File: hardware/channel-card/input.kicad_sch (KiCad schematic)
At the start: 50 parts, among them J1 INPUT MODULE, SW1 LOW-CUT (latching), U1 AD8273, U2 NE5532, U3 NE5532, U4 DG413DY

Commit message: Redraw filter and input sheets with wires; low-cut to 100 Hz
Filter and Input sheets are now drawn with real wires inside each
circuit block, generated by filter_wired.py and input_wired.py and
checked pin by pin against reference netlists (the Input reference is
frozen in scripts/reference). SSI2144 symbol rearranged so the ladder
capacitors sit beside their pins. Obsolete label-only post scripts
removed. The input low-cut moves to 100 Hz with 24k/47k resistors
(decision 73).

Co-Authored-By: Claude Opus 5.5 <noreply@anthropic.com>
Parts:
- R11, R13: value 16k -> 24k; ProjectPN SX-R-005 -> SX-R-031
- R12, R14: value 33k -> 47k; ProjectPN SX-R-006 -> SX-R-032
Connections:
- net LC_LED: no longer names the net of D5.2 (A), R18.2
- net LC_LEDK: no longer names the net of D5.1 (K), SW1.4 (A)
- net L_CPL: no longer names the net of C5.2, R5.1
- net L_HA: no longer names the net of C10.1, C9.2, R11.1
- net L_HB: no longer names the net of C10.2, R12.1, U3.3 (+)
- net L_HP: no longer names the net of R11.2, U3.1, U3.2 (-), U4.3
- net L_N: no longer names the net of C2.1, R2.2, U1.3 (+INA)
- net L_P: no longer names the net of C1.1, R1.2, U1.2 (-INA)
- net L_RX: no longer names the net of C5.1, U1.12 (SENSEA), U1.13 (OUTA)
- net L_SUM: no longer names the net of C7.1, D2.1 (K), R5.2, R7.1, U2.2 (-)
- net L_Z: no longer names the net of D1.1 (K), R9.2
- net R_CPL: no longer names the net of C6.2, R6.1
- net R_HA: no longer names the net of C11.2, C12.1, R13.1
- net R_HB: no longer names the net of C12.2, R14.1, U3.5 (+)
- net R_HP: no longer names the net of R13.2, U3.6 (-), U3.7, U4.6
- net R_N: no longer names the net of C4.1, R4.2, U1.5 (+INB)
- net R_P: no longer names the net of C3.1, R3.2, U1.6 (-INB)
- net R_RX: no longer names the net of C6.1, U1.10 (SENSEB), U1.9 (OUTB)
- net R_SUM: no longer names the net of C8.1, D4.1 (K), R6.2, R8.1, U2.6 (-)
- net R_Z: no longer names the net of D3.1 (K), R10.2
- no-connect marks 4 -> 6

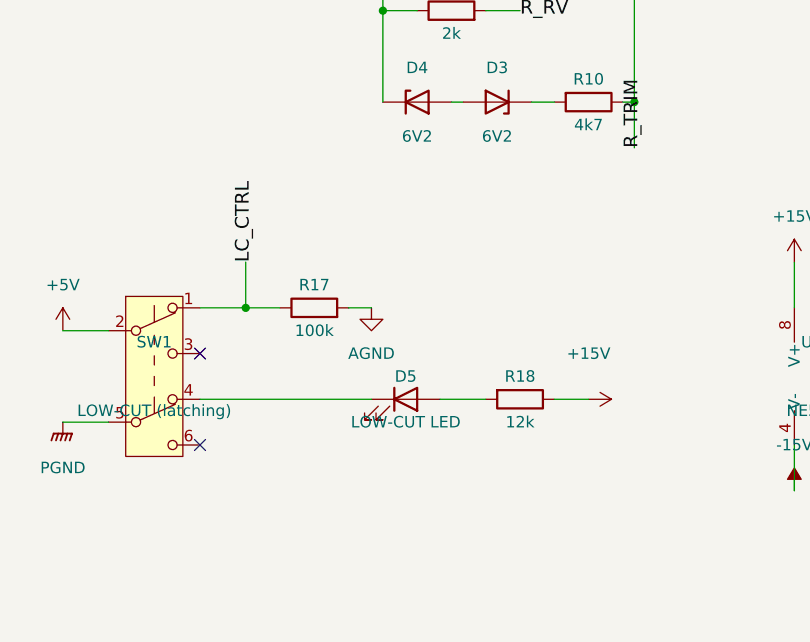
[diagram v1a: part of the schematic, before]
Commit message: Choose GPBS850N latching buttons with printed light caps
Buttons are CW Industries GPBS850N latching DPDT switches (Electrokit)
with 0805 LEDs lighting 3D-printed translucent caps (decision 75).
The datasheet shows pins 2-3 and 5-6 close when pressed, so every
button now uses pin 3 for logic and pin 6 for the LED. Adds the switch
footprint library, rebuild_all.sh, the state-retention requirement for
the momentary-button backlog item, and ten switches to the second
Electrokit order.

Co-Authored-By: Claude Opus 5.5 <noreply@anthropic.com>
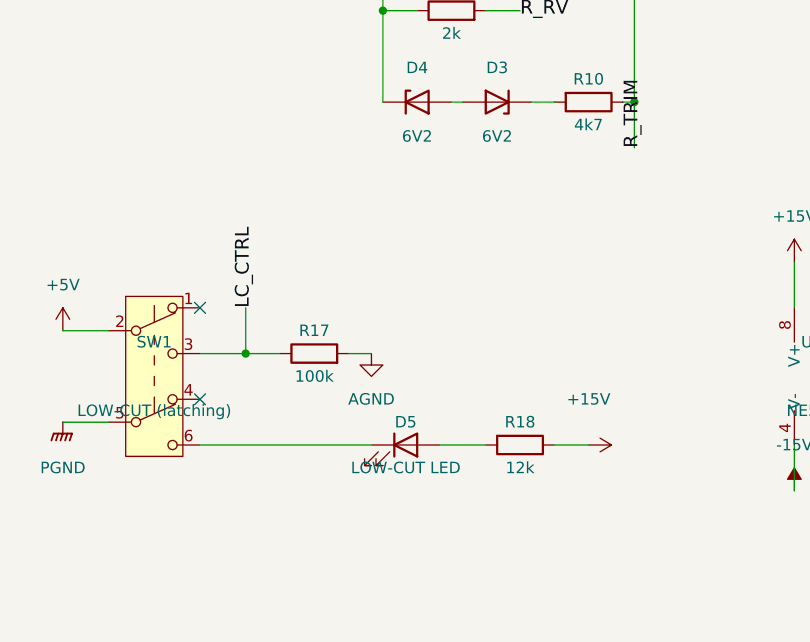
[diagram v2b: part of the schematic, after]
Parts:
- D5: footprint LED_THT:LED_D3.0mm -> LED_SMD:LED_0805_2012Metric
- SW1: footprint (none) -> syntsamix:SW_Latching_8.5x8.5mm_CW_GPBS850N; MPN (none) -> GPBS850N; Manufacturer (none) -> CW Industries; Supplier (none) -> Electrokit; SupplierPN (none) -> 41012905
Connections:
- net LC_CTRL: now also SW1.3 (C); no longer SW1.1 (A)
- net at D5.1 (K): now also SW1.6 (C); no longer SW1.4 (A)

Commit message: Add test pads to the channel card sheets
24 bare 1.5 mm test pads on key audio, control and ground nets across
the Input, Filter, Level, Routing and Meter sheets, named by net and
kept out of the BOM (decision 77). Each pad is in the reference
netlists, so the checks prove it sits on the intended net.

Co-Authored-By: Claude Opus 5.5 <noreply@anthropic.com>
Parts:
- added TP1: L_RX, TestPoint:TestPoint_Pad_D1.5mm, symbol Connector:TestPoint
- added TP2: L_TRIM, TestPoint:TestPoint_Pad_D1.5mm, symbol Connector:TestPoint
- added TP3: L_PREFILT, TestPoint:TestPoint_Pad_D1.5mm, symbol Connector:TestPoint
- added TP4: R_RX, TestPoint:TestPoint_Pad_D1.5mm, symbol Connector:TestPoint
- added TP5: R_TRIM, TestPoint:TestPoint_Pad_D1.5mm, symbol Connector:TestPoint
- added TP6: R_PREFILT, TestPoint:TestPoint_Pad_D1.5mm, symbol Connector:TestPoint
- added TP7: AGND, TestPoint:TestPoint_Pad_D1.5mm, symbol Connector:TestPoint
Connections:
- net AGND: now also TP7.1
- net L_PREFILT: now also TP3.1
- net L_TRIM: now also TP2.1
- net R_PREFILT: now also TP6.1
- net R_TRIM: now also TP5.1
- net at C5.1, U1.12 (SENSEA), U1.13 (OUTA): now also TP1.1
- net at C6.1, U1.10 (SENSEB), U1.9 (OUTB): now also TP4.1

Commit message: Channel card: draw decisions 97 and 98, fader buffer on an OPA2171 (decision 102)
- Level: SC_ENV into the summer's virtual earth through R217 30k1, R218 removed,
  summer + input on AGND (decision 97)
- Q301 emitter and button pull-downs R17, R186, R220, R222, R313, R315, R317 to PGND (decision 98)
- U204 = OPA2171 for the fader buffer and control summer (input range includes V-);
  superdiodes moved to the TL072 U205 (decision 102)
- simulation/level: fader law within 1.2 dB, ducking 10.07 dB per -1 V at every fader position
- Power budget, parts list, STATUS, breadboard test 10 and working notes updated

Co-Authored-By: Claude Opus 5.5 <noreply@anthropic.com>
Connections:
- net AGND: no longer R17.2
- net PGND: now also R17.2

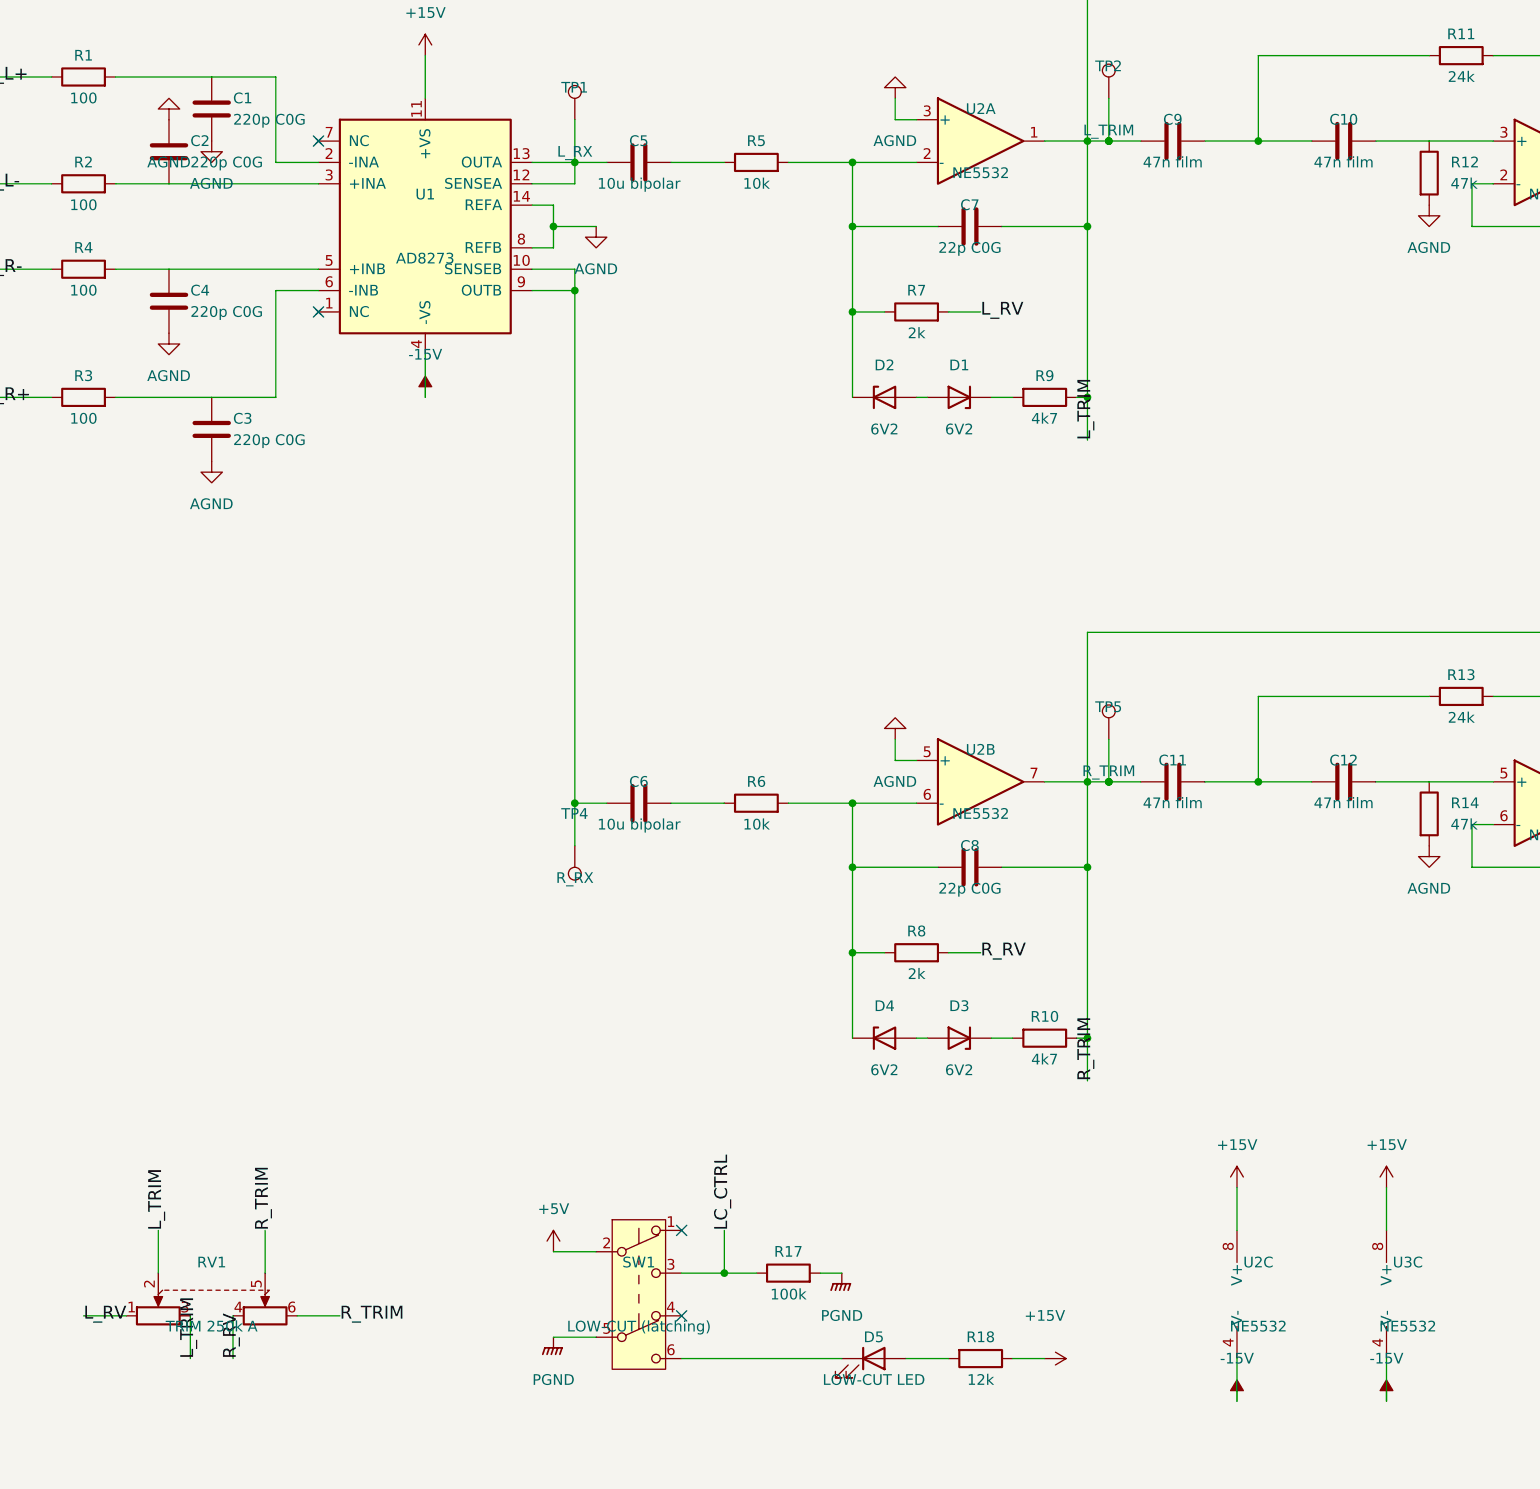
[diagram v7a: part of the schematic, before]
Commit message: Channel card: mechanical parts, decisions 110-117
- 110 LM317/LM337 in D2PAK on copper (onsemi, LCSC)
- 111 SMD electrolytics <= 5.4 mm (ROQANG, Panasonic bipolar)
- 112 trimmers and jumper headers on the underside, bottom cover for /system
- 113 low-cut caps C0G 1206
- 114 pot shaft standard T18 15 mm; 115 trim stage scaled to 100k, pots chosen
  (blocked until RoHS declarations)
- 116 RoHS strict for every part and board (process)
- 117 button LED colours (JLCPCB basic 0805), Wurth chain headers
- J181 drawn as Thonkiconn 3.5 mm (pending /system), fields and footprints set,
  five sheets rebuilt, netlists match, ERC 0/0
- STATUS: seven For /system items (CV jack, 0805 meter bezel, panel screws,
  bottom cover, underside keep-out, RoHS invariant, contract doc updates)

Co-Authored-By: Claude Opus 5.5 <noreply@anthropic.com>
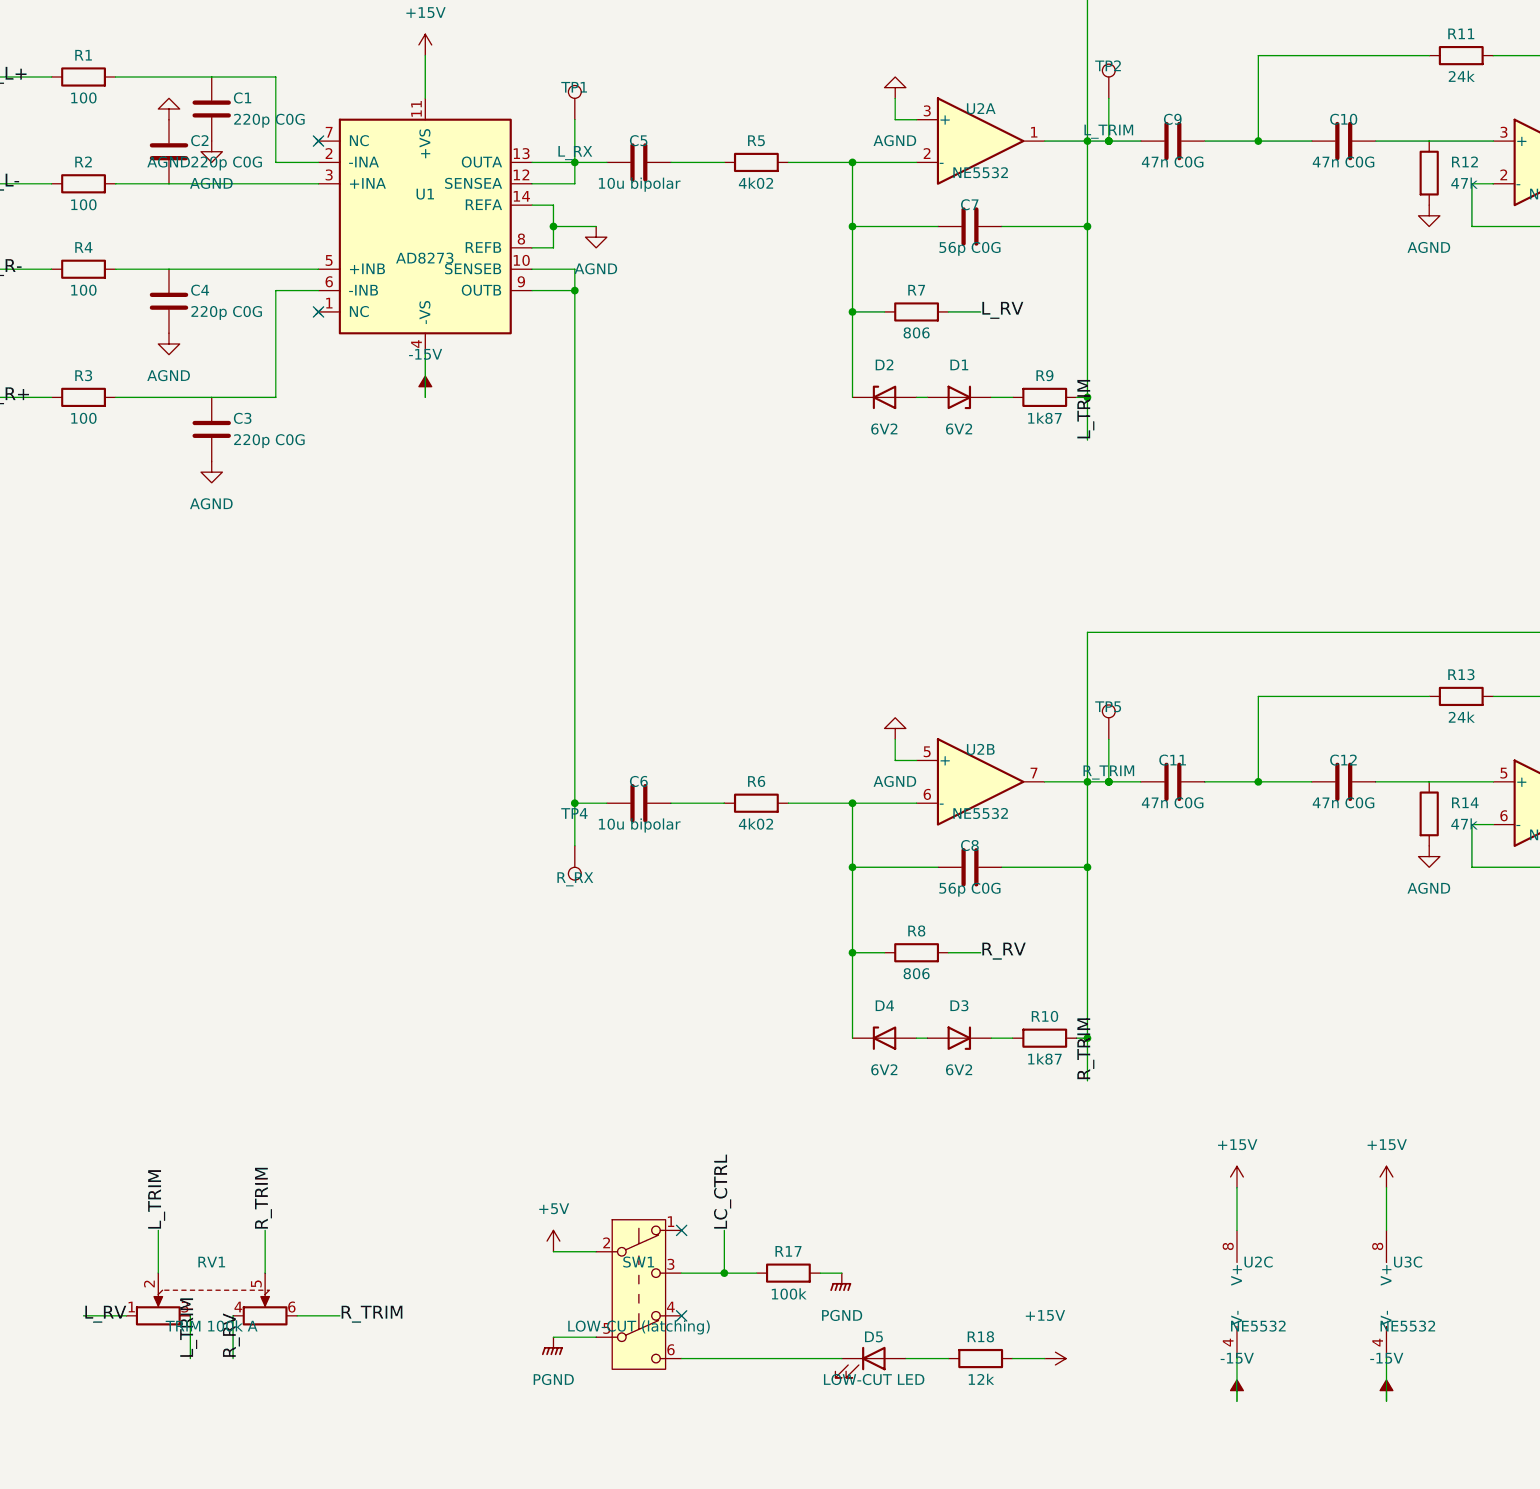
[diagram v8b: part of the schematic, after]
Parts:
- C10, C11, C12, C9: value 47n film -> 47n C0G; footprint Capacitor_THT:C_Rect_L7.2mm_W2.5mm_P5.00mm_FKS2_FKP2_MKS2_MKP2 -> Capacitor_SMD:C_1206_3216Metric; MPN (none) -> GRM31M5C1H473JA01L; Manufacturer (none) -> Murata; ProjectPN SX-C-005 -> SX-C-026; Supplier (none) -> LCSC; SupplierPN (none) -> C21812
- C5, C6: footprint Capacitor_THT:C_Radial_D5.0mm_H11.0mm_P2.00mm -> Capacitor_SMD:C_Elec_6.3x5.4; MPN (none) -> EEE-1VA100NP; Manufacturer (none) -> Panasonic; ProjectPN SX-C-003 -> SX-C-023; Supplier (none) -> Mouser; SupplierPN (none) -> 667-EEE-1VA100NP
- C7, C8: value 22p C0G -> 56p C0G; ProjectPN SX-C-004 -> SX-C-027
- D5: MPN (none) -> KT-0805W; Manufacturer (none) -> Hubei KENTO; ProjectPN SX-D-002 -> SX-D-017; Supplier (none) -> LCSC; SupplierPN (none) -> C34499
- R10, R9: value 4k7 -> 1k87; ProjectPN SX-R-004 -> SX-R-079
- R5, R6: value 10k -> 4k02; ProjectPN SX-R-002 -> SX-R-038
- R7, R8: value 2k -> 806; ProjectPN SX-R-003 -> SX-R-088
- RV1: value TRIM 250k A -> TRIM 100k A; ProjectPN SX-POT-002 -> SX-POT-011; Supplier (none) -> Thonk
